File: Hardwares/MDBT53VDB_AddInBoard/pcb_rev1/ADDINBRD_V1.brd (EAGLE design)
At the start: 25 x 40 mm, 22 parts, among them CN1 51296-0894, CN2 IF_6PIN, CN3 IF_3PIN, CN4 IF_5PIN_H, CN5 IF_2PIN_H, Q1 BSS84AKQBZ, SW1 SKTADAE010, U1 RV-3028-C7

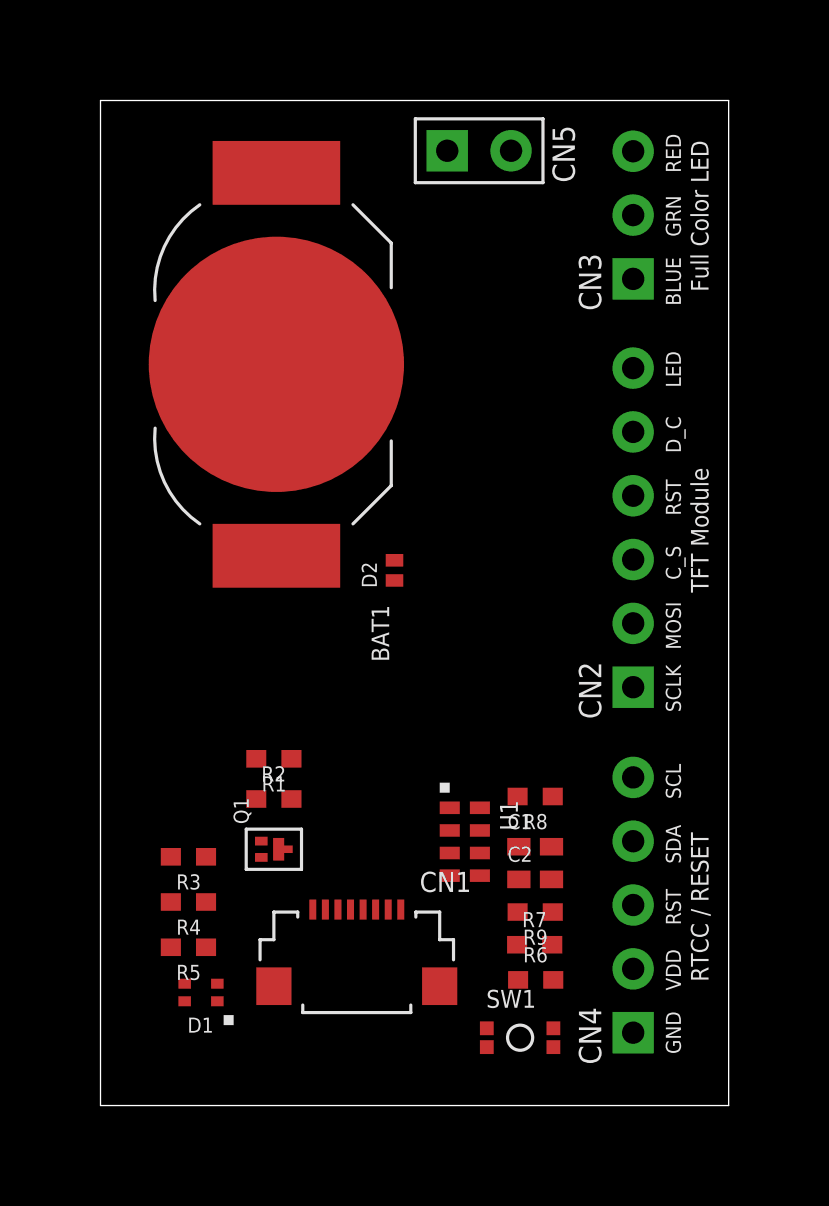
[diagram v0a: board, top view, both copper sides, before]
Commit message: レイアウトを修正
・部品、シルク位置を修正
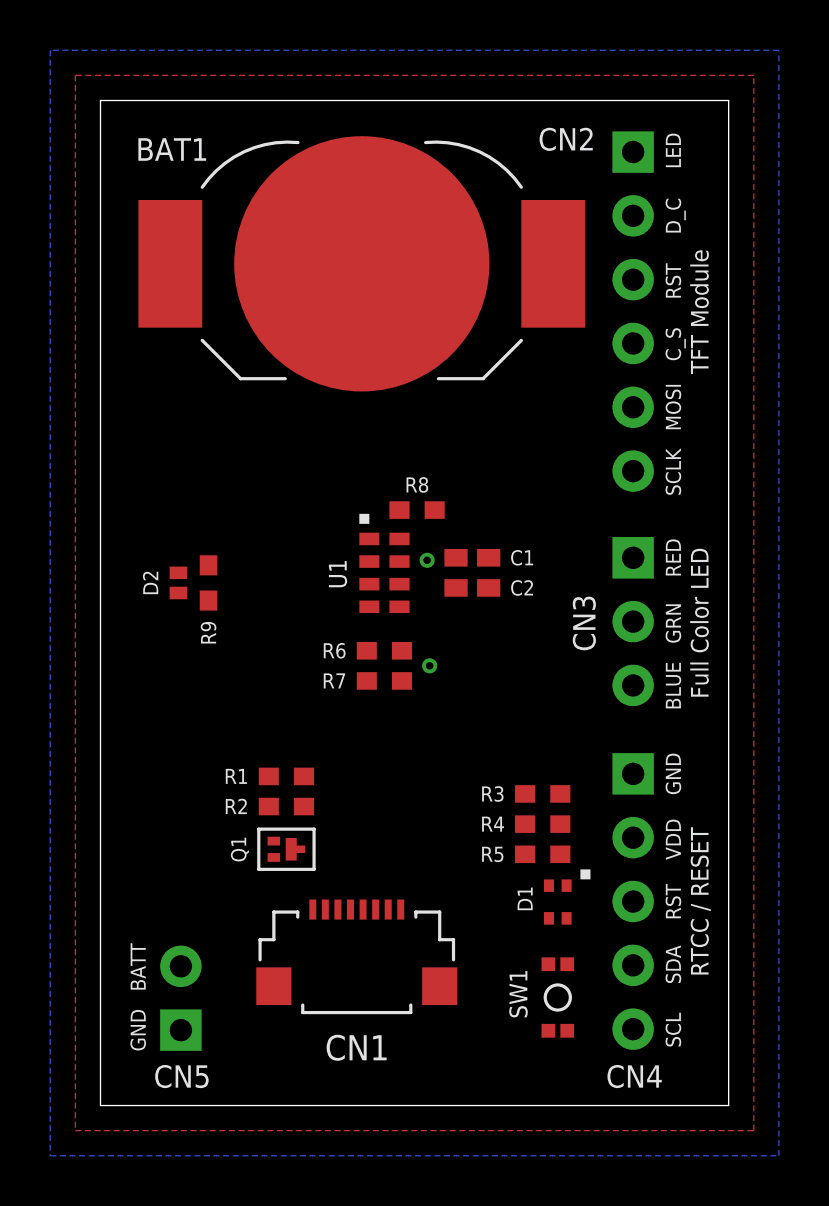
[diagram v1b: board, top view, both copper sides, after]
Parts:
- CN5: value IF_2PIN_H -> IF_2PIN
- moved CN5 36.6 mm to (3.20, 3.00), turned to 90 degrees
- moved R9 18.5 mm to (4.30, 20.8), turned to 90 degrees
- moved D1 14.6 mm to (18.2, 8.10), turned to 270 degrees
- moved R5 14.6 mm to (17.6, 10.0)
- moved R4 14.4 mm to (17.6, 11.2)
- moved R6 14.4 mm to (11.3, 18.1)
- moved R3 14.3 mm to (17.6, 12.4)
- moved R8 12.3 mm to (12.6, 23.7)
- moved R7 12.1 mm to (11.3, 16.9)
- moved C2 11.9 mm to (14.8, 20.6)
- moved C1 11.8 mm to (14.8, 21.8)
- moved U1 11.2 mm to (10.3, 22.8)
- moved CN3 11.1 mm to (21.2, 21.8), turned to 270 degrees
- moved CN4 10.3 mm to (21.2, 13.2), turned to 270 degrees
- moved D2 8.61 mm to (3.10, 20.8)
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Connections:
- net 0V: now also CN5.1; no longer CN5.2
- net N$2: now also CN5.2; no longer CN5.1
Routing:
- added copper zone on layer 1, net 0V
- added copper zone on layer 16, net 0V
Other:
- board text added: "BATT"

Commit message: レイアウトを修正
・３色LED、リセットボタンの配線
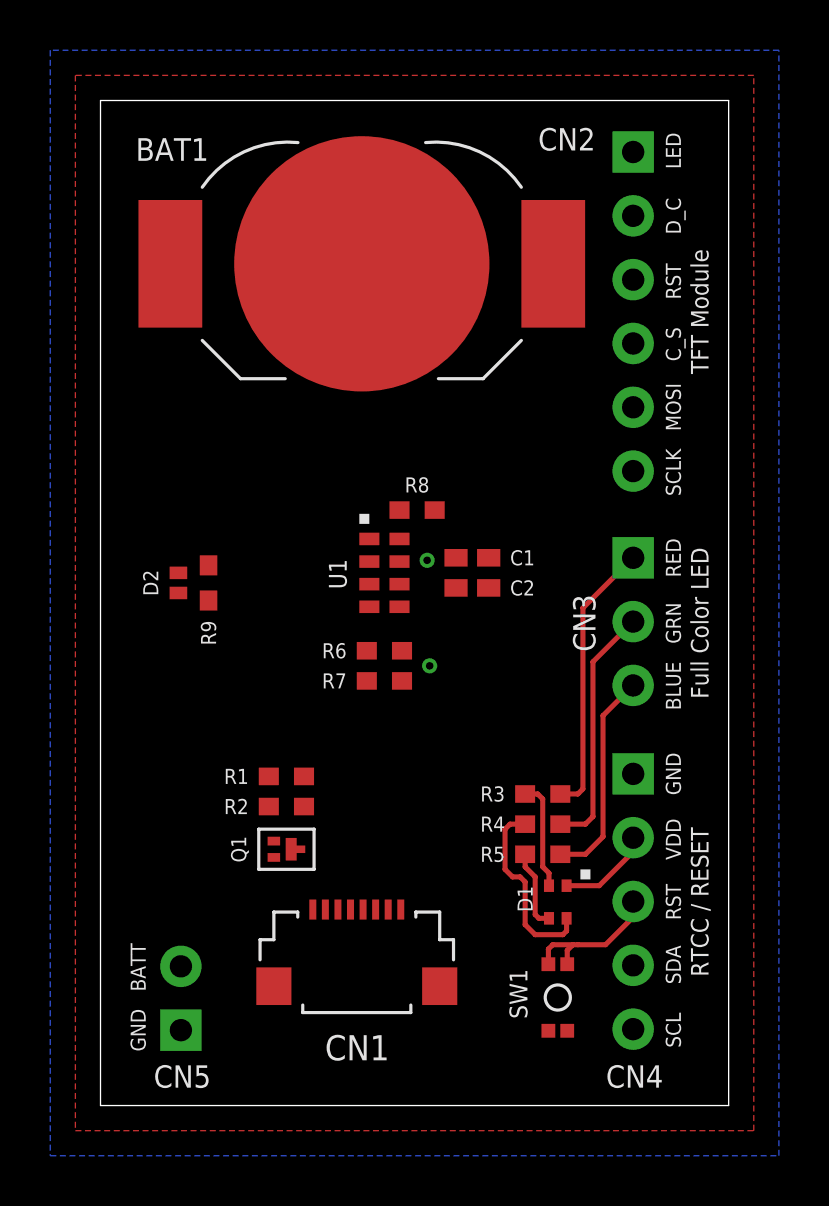
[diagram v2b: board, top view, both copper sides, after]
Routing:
- net LED_R: track 0.00 -> 11.0 mm
- net LED_G: track 0.00 -> 9.85 mm
- net LED_B: track 0.00 -> 8.51 mm
- net N$5: track 0.00 -> 7.57 mm
- net RESET_NRF: track 0.00 -> 5.99 mm
- net N$6: track 0.00 -> 4.34 mm
- net VDD: track 0.00 -> 3.77 mm
- net N$10: track 0.00 -> 3.18 mm
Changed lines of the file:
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@@
 <setting verticaltext="up"/>
 </settings>
-<grid distance="1" unitdist="mm" unit="mm" style="lines" multiple="1" display="yes" altdistance="0.025" altunitdist="inch" altunit="inch"/>
+<grid distance="0.1" unitdist="mm" unit="mm" style="lines" multiple="1" display="yes" altdistance="0.025" altunitdist="inch" altunit="inch"/>
 <layers>
 <layer number="1" name="Top" color="4" fill="1" visible="yes" active="yes"/>
@@
 <via x="13.1" y="17.5" extent="1-16" drill="0.3"/>
 <via x="13" y="21.7" extent="1-16" drill="0.3"/>
+<wire x1="18.55" y1="8.75" x2="19.85" y2="8.75" width="0.2032" layer="1"/>
+<wire x1="21.2" y1="10.66" x2="21.2" y2="10.1" width="0.2032" layer="1"/>
+<wire x1="21.2" y1="10.1" x2="19.85" y2="8.75" width="0.2032" layer="1"/>
 <wire x1="13" y1="21.7" x2="14.15" y2="21.8" width="0" layer="19" extent="1-1"/>
 <wire x1="11.9" y1="21.65" x2="13" y2="21.7" width="0" layer="19" extent="1-1"/>
@@
 <wire x1="11.45" y1="7.8" x2="6.9" y2="9.875" width="0" layer="19" extent="1-1"/>
 <wire x1="18.55" y1="8.75" x2="11.45" y2="7.8" width="0" layer="19" extent="1-1"/>
-<wire x1="21.2" y1="10.66" x2="18.55" y2="8.75" width="0" layer="19" extent="1-1"/>
 </signal>
 <signal name="LED_CTRL">
@@
 <contactref element="CN3" pad="1"/>
 <contactref element="R3" pad="1"/>
-<wire x1="18.3" y1="12.4" x2="21.2" y2="21.8" width="0" layer="19" extent="1-1"/>
+<wire x1="18.3" y1="12.4" x2="19" y2="12.4" width="0.2032" layer="1"/>
+<wire x1="19" y1="12.4" x2="19.2" y2="12.6" width="0.2032" layer="1"/>
+<wire x1="19.2" y1="12.6" x2="19.2" y2="19.8" width="0.2032" layer="1"/>
+<wire x1="19.2" y1="19.8" x2="21.2" y2="21.8" width="0.2032" layer="1"/>
 </signal>
 <signal name="LED_G">
 <contactref element="CN3" pad="2"/>
 <contactref element="R4" pad="1"/>
-<wire x1="18.3" y1="11.2" x2="21.2" y2="19.26" width="0" layer="19" extent="1-1"/>
+<wire x1="18.3" y1="11.2" x2="19.3" y2="11.2" width="0.2032" layer="1"/>
+<wire x1="19.3" y1="11.2" x2="19.6" y2="11.5" width="0.2032" layer="1"/>
+<wire x1="19.6" y1="11.5" x2="19.6" y2="17.66" width="0.2032" layer="1"/>
+<wire x1="19.6" y1="17.66" x2="21.2" y2="19.26" width="0.2032" layer="1"/>
 </signal>
 <signal name="LED_B">
 <contactref element="CN3" pad="3"/>
 <contactref element="R5" pad="1"/>
-<wire x1="18.3" y1="10" x2="21.2" y2="16.72" width="0" layer="19" extent="1-1"/>
+<wire x1="18.3" y1="10" x2="19.3" y2="10" width="0.2032" layer="1"/>
+<wire x1="19.3" y1="10" x2="20" y2="10.7" width="0.2032" layer="1"/>
+<wire x1="20" y1="10.7" x2="20" y2="15.52" width="0.2032" layer="1"/>
+<wire x1="20" y1="15.52" x2="21.2" y2="16.72" width="0.2032" layer="1"/>
 </signal>
 <signal name="N$6">
 <contactref element="D1" pad="2"/>
 <contactref element="R3" pad="2"/>
-<wire x1="16.9" y1="12.4" x2="17.85" y2="8.75" width="0" layer="19" extent="1-1"/>
+<wire x1="17.85" y1="8.75" x2="17.85" y2="9.25" width="0.2032" layer="1"/>
+<wire x1="17.85" y1="9.25" x2="17.6" y2="9.5" width="0.2032" layer="1"/>
+<wire x1="17.6" y1="9.5" x2="17.6" y2="12.2" width="0.2032" layer="1"/>
+<wire x1="17.6" y1="12.2" x2="17.4" y2="12.4" width="0.2032" layer="1"/>
+<wire x1="17.4" y1="12.4" x2="16.9" y2="12.4" width="0.2032" layer="1"/>
 </signal>
 <signal name="N$10">
 <contactref element="D1" pad="3"/>
 <contactref element="R5" pad="2"/>
-<wire x1="16.9" y1="10" x2="17.85" y2="7.45" width="0" layer="19" extent="1-1"/>
+<wire x1="17.85" y1="7.45" x2="17.45" y2="7.45" width="0.2032" layer="1"/>
+<wire x1="17.45" y1="7.45" x2="17.3" y2="7.6" width="0.2032" layer="1"/>
+<wire x1="17.3" y1="7.6" x2="17.3" y2="9.1" width="0.2032" layer="1"/>
+<wire x1="17.3" y1="9.1" x2="16.9" y2="9.5" width="0.2032" layer="1"/>
+<wire x1="16.9" y1="10" x2="16.9" y2="9.5" width="0.2032" layer="1"/>
 </signal>
 <signal name="N$5">
 <contactref element="D1" pad="4"/>
 <contactref element="R4" pad="2"/>
-<wire x1="18.55" y1="7.45" x2="16.9" y2="11.2" width="0" layer="19" extent="1-1"/>
+<wire x1="18.55" y1="7.45" x2="18.55" y2="6.95" width="0.2032" layer="1"/>
+<wire x1="18.55" y1="6.95" x2="18.4" y2="6.8" width="0.2032" layer="1"/>
+<wire x1="18.4" y1="6.8" x2="17.3" y2="6.8" width="0.2032" layer="1"/>
+<wire x1="17.3" y1="6.8" x2="16.9" y2="7.2" width="0.2032" layer="1"/>
+<wire x1="16.9" y1="7.2" x2="16.9" y2="8.9" width="0.2032" layer="1"/>
+<wire x1="16.9" y1="8.9" x2="16.7" y2="9.1" width="0.2032" layer="1"/>
+<wire x1="16.7" y1="9.1" x2="16.4" y2="9.1" width="0.2032" layer="1"/>
+<wire x1="16.4" y1="9.1" x2="16.1" y2="9.4" width="0.2032" layer="1"/>
+<wire x1="16.1" y1="9.4" x2="16.1" y2="11" width="0.2032" layer="1"/>
+<wire x1="16.1" y1="11" x2="16.3" y2="11.2" width="0.2032" layer="1"/>
+<wire x1="16.3" y1="11.2" x2="16.9" y2="11.2" width="0.2032" layer="1"/>
 </signal>
 <signal name="TWI_SDA">
@@
 <contactref element="SW1" pad="1"/>
 <contactref element="SW1" pad="3"/>
-<wire x1="18.575" y1="5.625" x2="21.2" y2="8.12" width="0" layer="19" extent="1-1"/>
-<wire x1="17.825" y1="5.625" x2="18.575" y2="5.625" width="0" layer="19" extent="1-1"/>
+<wire x1="18.575" y1="5.625" x2="18.575" y2="6.175" width="0.2032" layer="1"/>
+<wire x1="18.575" y1="6.175" x2="18.8" y2="6.4" width="0.2032" layer="1"/>
+<wire x1="18.8" y1="6.4" x2="19" y2="6.4" width="0.2032" layer="1"/>
+<wire x1="19" y1="6.4" x2="20.1" y2="6.4" width="0.2032" layer="1"/>
+<wire x1="20.1" y1="6.4" x2="21.2" y2="7.5" width="0.2032" layer="1"/>
+<wire x1="21.2" y1="8.12" x2="21.2" y2="7.5" width="0.2032" layer="1"/>
+<wire x1="17.825" y1="5.625" x2="17.825" y2="6.225" width="0.2032" layer="1"/>
+<wire x1="17.825" y1="6.225" x2="18" y2="6.4" width="0.2032" layer="1"/>
+<wire x1="18" y1="6.4" x2="18.8" y2="6.4" width="0.2032" layer="1"/>
 </signal>
 <signal name="N$2">

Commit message: レイアウトを修正
・TFTモジュール周りの配線
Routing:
- net LED_CTRL: track 0.00 -> 37.5 mm
- net D_C: track 0.00 -> 34.2 mm, vias 0 -> 1
- net RESET: track 0.00 -> 32.6 mm, vias 0 -> 1
- net CS: track 0.00 -> 27.7 mm
- net MOSI: track 0.00 -> 27.1 mm, vias 0 -> 1
- net CLK: track 0.00 -> 25.7 mm, vias 0 -> 1
- net LEDA: track 0.00 -> 0.75 mm
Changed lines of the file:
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@@
 <contactref element="CN1" pad="1"/>
 <contactref element="Q1" pad="3"/>
-<wire x1="7.59" y1="10.2" x2="8.45" y2="7.8" width="0" layer="19" extent="1-1"/>
+<wire x1="8.45" y1="7.8" x2="8.45" y2="8.55" width="0.2032" layer="1"/>
+<wire x1="8.45" y1="8.55" x2="7.59" y2="10.2" width="0" layer="19" extent="1-1"/>
 </signal>
 <signal name="0V">
@@
 <contactref element="R1" pad="1"/>
 <contactref element="CN2" pad="1"/>
-<wire x1="8.1" y1="13.1" x2="21.2" y2="37.95" width="0" layer="19" extent="1-1"/>
+<wire x1="21.2" y1="37.95" x2="21.2" y2="37" width="0.2032" layer="1"/>
+<wire x1="21.2" y1="37" x2="20" y2="35.8" width="0.2032" layer="1"/>
+<wire x1="20" y1="35.8" x2="20" y2="30.3" width="0.2032" layer="1"/>
+<wire x1="20" y1="30.3" x2="17.4" y2="27.7" width="0.2032" layer="1"/>
+<wire x1="17.4" y1="27.7" x2="17.4" y2="25.1" width="0.2032" layer="1"/>
+<wire x1="17.4" y1="25.1" x2="17.8" y2="24.7" width="0.2032" layer="1"/>
+<wire x1="17.8" y1="24.7" x2="17.8" y2="22.1" width="0.2032" layer="1"/>
+<wire x1="17.8" y1="22.1" x2="16.8" y2="21.1" width="0.2032" layer="1"/>
+<wire x1="16.8" y1="21.1" x2="16.8" y2="15.4" width="0.2032" layer="1"/>
+<wire x1="16.8" y1="15.4" x2="16.6" y2="15.2" width="0.2032" layer="1"/>
+<wire x1="16.6" y1="15.2" x2="15.4" y2="15.2" width="0.2032" layer="1"/>
+<wire x1="15.4" y1="15.2" x2="14.1" y2="13.9" width="0.2032" layer="1"/>
+<wire x1="14.1" y1="13.9" x2="14.1" y2="12.6" width="0.2032" layer="1"/>
+<wire x1="14.1" y1="12.6" x2="12.3" y2="10.8" width="0.2032" layer="1"/>
+<wire x1="12.3" y1="10.8" x2="10.4" y2="10.8" width="0.2032" layer="1"/>
+<wire x1="10.4" y1="10.8" x2="9.4" y2="11.8" width="0.2032" layer="1"/>
+<wire x1="9.4" y1="11.8" x2="9.4" y2="12.6" width="0.2032" layer="1"/>
+<wire x1="9.4" y1="12.6" x2="8.9" y2="13.1" width="0.2032" layer="1"/>
+<wire x1="8.1" y1="13.1" x2="8.9" y2="13.1" width="0.2032" layer="1"/>
 </signal>
 <signal name="CS">
 <contactref element="CN1" pad="8"/>
 <contactref element="CN2" pad="4"/>
-<wire x1="11.95" y1="7.8" x2="21.2" y2="30.33" width="0" layer="19" extent="1-1"/>
+<wire x1="11.95" y1="7.8" x2="11.95" y2="8.55" width="0.2032" layer="1"/>
+<wire x1="11.95" y1="8.55" x2="12.2" y2="8.8" width="0.2032" layer="1"/>
+<wire x1="12.2" y1="8.8" x2="13.3" y2="8.8" width="0.2032" layer="1"/>
+<wire x1="16.1" y1="11.6" x2="16.1" y2="12.9" width="0.2032" layer="1"/>
+<wire x1="16.1" y1="12.9" x2="16.4" y2="13.2" width="0.2032" layer="1"/>
+<wire x1="21.2" y1="30.33" x2="21.2" y2="29.7" width="0.2032" layer="1"/>
+<wire x1="21.2" y1="29.7" x2="19.8" y2="28.3" width="0.2032" layer="1"/>
+<wire x1="19.8" y1="28.3" x2="19.8" y2="21.1" width="0.2032" layer="1"/>
+<wire x1="19.8" y1="21.1" x2="18.8" y2="20.1" width="0.2032" layer="1"/>
+<wire x1="18.8" y1="20.1" x2="18.8" y2="14.4" width="0.2032" layer="1"/>
+<wire x1="16.4" y1="13.2" x2="17.6" y2="13.2" width="0.2032" layer="1"/>
+<wire x1="18.8" y1="14.4" x2="17.6" y2="13.2" width="0.2032" layer="1"/>
+<wire x1="13.3" y1="8.8" x2="16.1" y2="11.6" width="0.2032" layer="1"/>
 </signal>
 <signal name="CLK">
 <contactref element="CN1" pad="6"/>
 <contactref element="CN2" pad="6"/>
-<wire x1="10.95" y1="7.8" x2="21.2" y2="25.25" width="0" layer="19" extent="1-1"/>
+<wire x1="10.95" y1="7.8" x2="10.95" y2="8.65" width="0.2032" layer="1"/>
+<wire x1="10.95" y1="8.65" x2="11.5" y2="9.2" width="0.2032" layer="1"/>
+<wire x1="11.5" y1="9.2" x2="13.1" y2="9.2" width="0.2032" layer="1"/>
+<wire x1="15.7" y1="11.8" x2="15.7" y2="13.1" width="0.2032" layer="1"/>
+<wire x1="15.7" y1="13.1" x2="16.2" y2="13.6" width="0.2032" layer="1"/>
+<wire x1="18.4" y1="14.6" x2="18.4" y2="20.3" width="0.2032" layer="1"/>
+<wire x1="18.4" y1="20.3" x2="19.4" y2="21.3" width="0.2032" layer="1"/>
+<via x="19.2" y="26" extent="1-16" drill="0.3"/>
+<wire x1="21.2" y1="25.25" x2="19.95" y2="25.25" width="0.2032" layer="16"/>
+<wire x1="19.95" y1="25.25" x2="19.2" y2="26" width="0.2032" layer="16"/>
+<wire x1="19.4" y1="21.3" x2="19.4" y2="25.8" width="0.2032" layer="1"/>
+<wire x1="19.4" y1="25.8" x2="19.2" y2="26" width="0.2032" layer="1"/>
+<wire x1="16.2" y1="13.6" x2="17.4" y2="13.6" width="0.2032" layer="1"/>
+<wire x1="17.4" y1="13.6" x2="18.4" y2="14.6" width="0.2032" layer="1"/>
+<wire x1="15.7" y1="11.8" x2="13.1" y2="9.2" width="0.2032" layer="1"/>
 </signal>
 <signal name="MOSI">
 <contactref element="CN1" pad="5"/>
 <contactref element="CN2" pad="5"/>
-<wire x1="10.45" y1="7.8" x2="21.2" y2="27.79" width="0" layer="19" extent="1-1"/>
+<via x="19.2" y="26.9" extent="1-16" drill="0.3"/>
+<wire x1="19.2" y1="26.9" x2="18.6" y2="26.3" width="0.2032" layer="1"/>
+<wire x1="18.6" y1="26.3" x2="18.6" y2="25.7" width="0.2032" layer="1"/>
+<wire x1="18.6" y1="25.7" x2="19" y2="25.3" width="0.2032" layer="1"/>
+<wire x1="21.2" y1="27.79" x2="20.09" y2="27.79" width="0.2032" layer="16"/>
+<wire x1="20.09" y1="27.79" x2="19.2" y2="26.9" width="0.2032" layer="16"/>
+<wire x1="10.45" y1="7.8" x2="10.45" y2="8.75" width="0.2032" layer="1"/>
+<wire x1="10.45" y1="8.75" x2="11.3" y2="9.6" width="0.2032" layer="1"/>
+<wire x1="11.3" y1="9.6" x2="12.9" y2="9.6" width="0.2032" layer="1"/>
+<wire x1="15.3" y1="12" x2="15.3" y2="13.3" width="0.2032" layer="1"/>
+<wire x1="15.3" y1="13.3" x2="16" y2="14" width="0.2032" layer="1"/>
+<wire x1="18" y1="14.8" x2="18" y2="20.5" width="0.2032" layer="1"/>
+<wire x1="18" y1="20.5" x2="19" y2="21.5" width="0.2032" layer="1"/>
+<wire x1="19" y1="21.5" x2="19" y2="25.3" width="0.2032" layer="1"/>
+<wire x1="16" y1="14" x2="17.2" y2="14" width="0.2032" layer="1"/>
+<wire x1="18" y1="14.8" x2="17.2" y2="14" width="0.2032" layer="1"/>
+<wire x1="12.9" y1="9.6" x2="15.3" y2="12" width="0.2032" layer="1"/>
 </signal>
 <signal name="D_C">
 <contactref element="CN1" pad="4"/>
 <contactref element="CN2" pad="2"/>
-<wire x1="9.95" y1="7.8" x2="21.2" y2="35.41" width="0" layer="19" extent="1-1"/>
+<via x="19.4" y="28.8" extent="1-16" drill="0.3"/>
+<wire x1="9.95" y1="7.8" x2="9.95" y2="8.85" width="0.2032" layer="1"/>
+<wire x1="9.95" y1="8.85" x2="11.1" y2="10" width="0.2032" layer="1"/>
+<wire x1="11.1" y1="10" x2="11.9" y2="10" width="0.2032" layer="1"/>
+<wire x1="11.9" y1="10" x2="12.4" y2="10" width="0.2032" layer="1"/>
+<wire x1="14.9" y1="12.2" x2="14.9" y2="13.5" width="0.2032" layer="1"/>
+<wire x1="14.9" y1="13.5" x2="15.8" y2="14.4" width="0.2032" layer="1"/>
+<wire x1="15.8" y1="14.4" x2="17" y2="14.4" width="0.2032" layer="1"/>
+<wire x1="17.6" y1="15" x2="17.6" y2="20.7" width="0.2032" layer="1"/>
+<wire x1="17.6" y1="20.7" x2="18.6" y2="21.7" width="0.2032" layer="1"/>
+<wire x1="18.6" y1="21.7" x2="18.6" y2="25.1" width="0.2032" layer="1"/>
+<wire x1="18.6" y1="25.1" x2="18.2" y2="25.5" width="0.2032" layer="1"/>
+<wire x1="18.2" y1="25.5" x2="18.2" y2="26.7" width="0.2032" layer="1"/>
+<wire x1="18.2" y1="26.7" x2="19.4" y2="27.9" width="0.2032" layer="1"/>
+<wire x1="19.4" y1="28.8" x2="19.6" y2="29" width="0.2032" layer="16"/>
+<wire x1="19.6" y1="29" x2="19.6" y2="30.9" width="0.2032" layer="16"/>
+<wire x1="19.6" y1="30.9" x2="20" y2="31.3" width="0.2032" layer="16"/>
+<wire x1="20" y1="31.3" x2="20" y2="33.3" width="0.2032" layer="16"/>
+<wire x1="21.2" y1="35.41" x2="21.2" y2="34.5" width="0.2032" layer="16"/>
+<wire x1="21.2" y1="34.5" x2="20" y2="33.3" width="0.2032" layer="16"/>
+<wire x1="19.4" y1="27.9" x2="19.4" y2="28.8" width="0.2032" layer="1"/>
+<wire x1="17.6" y1="15" x2="17" y2="14.4" width="0.2032" layer="1"/>
+<wire x1="14.9" y1="12.2" x2="12.7" y2="10" width="0.2032" layer="1"/>
+<wire x1="12.7" y1="10" x2="12.4" y2="10" width="0.2032" layer="1"/>
 </signal>
 <signal name="RESET">
 <contactref element="CN1" pad="3"/>
 <contactref element="CN2" pad="3"/>
-<wire x1="9.45" y1="7.8" x2="21.2" y2="32.87" width="0" layer="19" extent="1-1"/>
+<via x="18.7" y="28.1" extent="1-16" drill="0.3"/>
+<wire x1="9.45" y1="7.8" x2="9.45" y2="8.95" width="0.2032" layer="1"/>
+<wire x1="9.45" y1="8.95" x2="10.9" y2="10.4" width="0.2032" layer="1"/>
+<wire x1="10.9" y1="10.4" x2="12.5" y2="10.4" width="0.2032" layer="1"/>
+<wire x1="12.5" y1="10.4" x2="14.5" y2="12.4" width="0.2032" layer="1"/>
+<wire x1="14.5" y1="12.4" x2="14.5" y2="13.7" width="0.2032" layer="1"/>
+<wire x1="14.5" y1="13.7" x2="15.6" y2="14.8" width="0.2032" layer="1"/>
+<wire x1="17.2" y1="15.2" x2="17.2" y2="20.9" width="0.2032" layer="1"/>
+<wire x1="17.2" y1="20.9" x2="18.2" y2="21.9" width="0.2032" layer="1"/>
+<wire x1="18.2" y1="21.9" x2="18.2" y2="24.9" width="0.2032" layer="1"/>
+<wire x1="18.2" y1="24.9" x2="17.8" y2="25.3" width="0.2032" layer="1"/>
+<wire x1="17.8" y1="25.3" x2="17.8" y2="27.2" width="0.2032" layer="1"/>
+<wire x1="17.8" y1="27.2" x2="18.7" y2="28.1" width="0.2032" layer="1"/>
+<wire x1="20" y1="28.3" x2="20" y2="30.7" width="0.2032" layer="16"/>
+<wire x1="21.2" y1="32.87" x2="21.2" y2="31.9" width="0.2032" layer="16"/>
+<wire x1="21.2" y1="31.9" x2="20" y2="30.7" width="0.2032" layer="16"/>
+<wire x1="18.7" y1="28.1" x2="19.8" y2="28.1" width="0.2032" layer="16"/>
+<wire x1="19.8" y1="28.1" x2="20" y2="28.3" width="0.2032" layer="16"/>
+<wire x1="15.6" y1="14.8" x2="16.8" y2="14.8" width="0.2032" layer="1"/>
+<wire x1="17.2" y1="15.2" x2="16.8" y2="14.8" width="0.2032" layer="1"/>
 </signal>
 <signal name="LED_R">
